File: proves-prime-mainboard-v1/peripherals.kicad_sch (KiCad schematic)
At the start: 38 parts, among them IC3 RV-3028-C7_32.768kHz_1ppm_TA_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, J6 Breakout, J7 Breakout, J8 Molex 503398-1892, U3 MCP25625-E/ML, U4 AP3602AKTR-G1, U5 LSM6DSOTR, U6 LSM303AGRTR, Y2 16MHZ 12 pf

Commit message: Migrated Temperature Sensor
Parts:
- added C38: 1uF, Capacitor_SMD:C_0805_2012Metric, symbol Device:C
- added U11: MCP9808T-E/MS, Package_SO:MSOP-8-1EP_3x3mm_P0.65mm_EP1.5x1.8mm_ThermalVias, symbol Sensor_Temperature:MCP9808_DFN
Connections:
- net +3V3: now also C38.1, U11.6 (A1), U11.7 (A0), U11.8 (VDD)
- net GND: now also C38.2, U11.4 (GND), U11.5 (A2), U11.9 (EP/GND)
- no-connect marks 23 -> 24
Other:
- moved on the sheet: C24, C25, C26, C27, C28, C31, C32, C33, C34, C35, D7, J6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

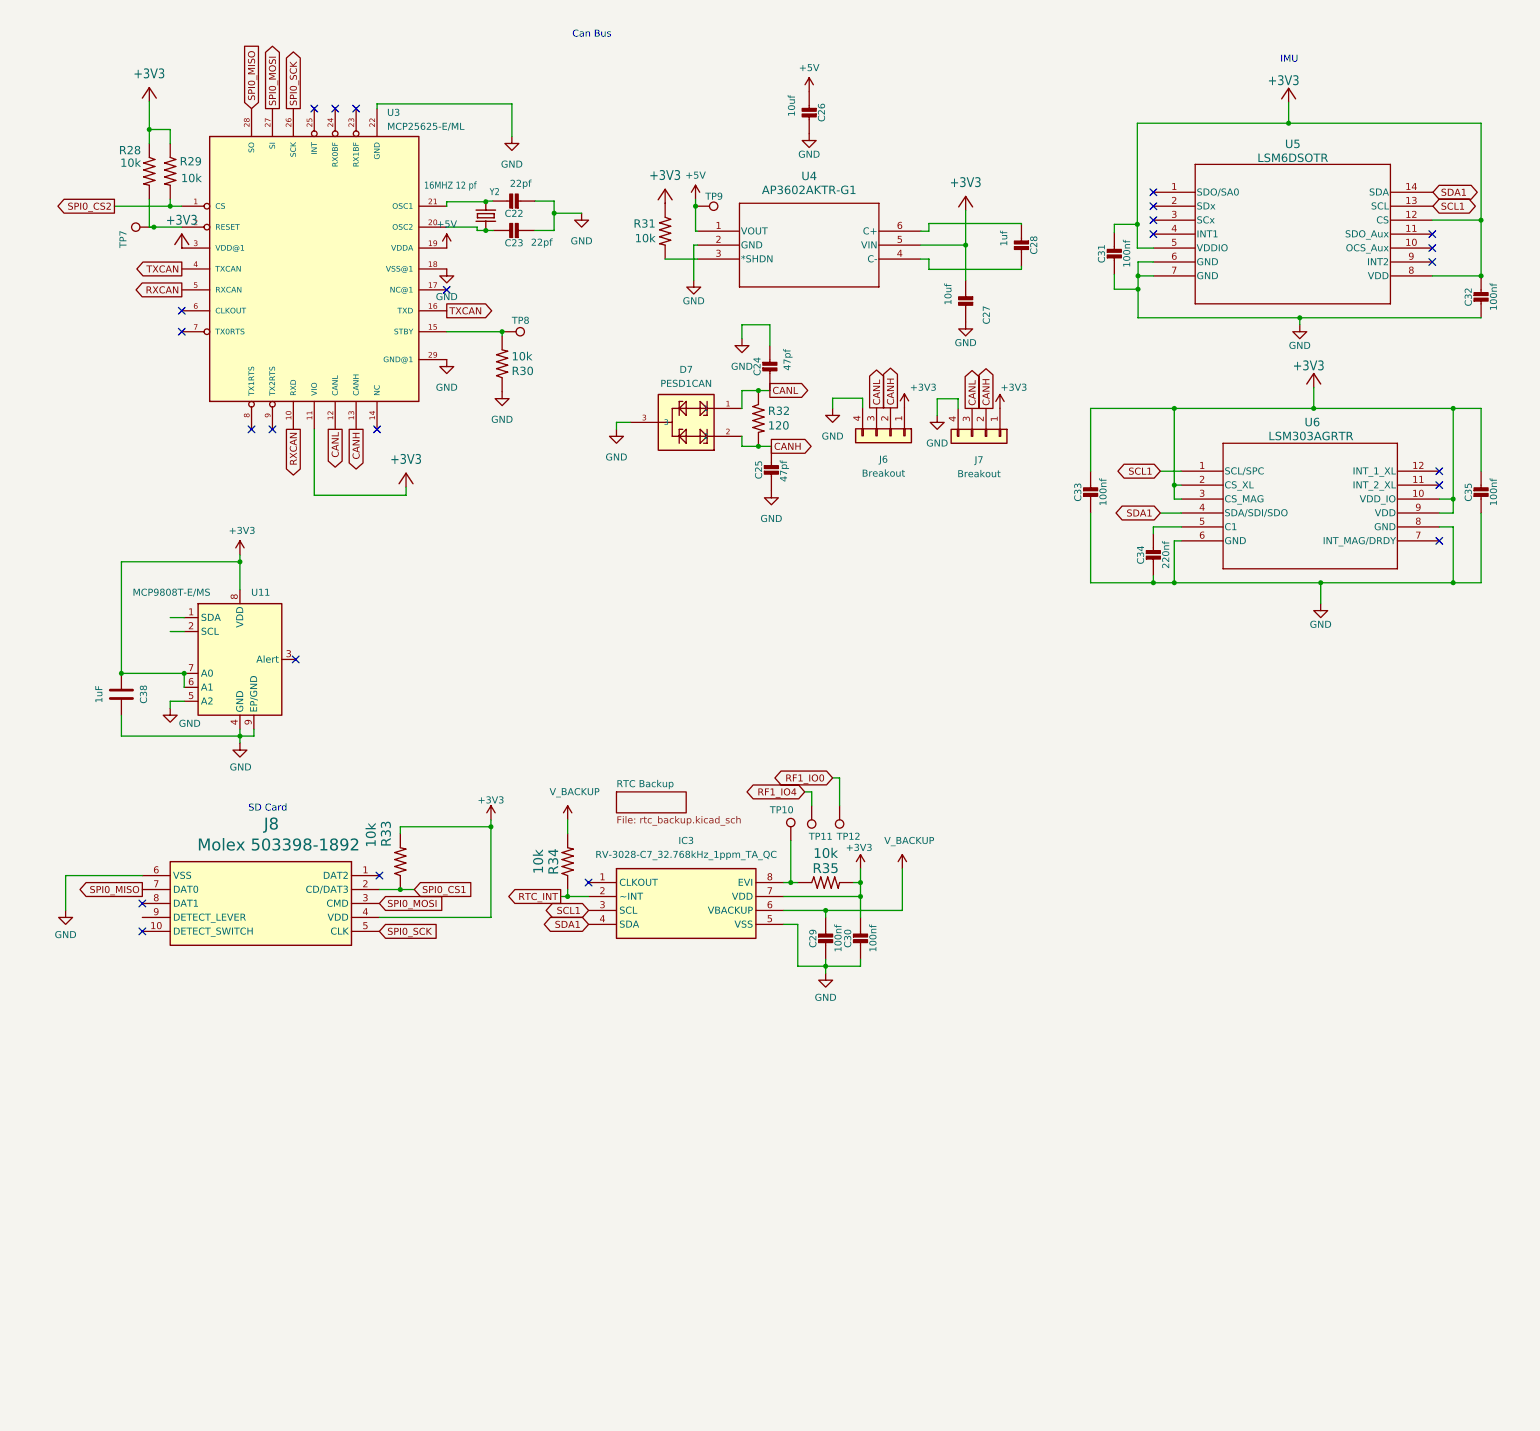
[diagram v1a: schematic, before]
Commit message: Added Voltage Regulators
LT8610 3v3 and 5v

Co-Authored-By: rrakushkin <128992626+rrakushkin@users.noreply.github.com>
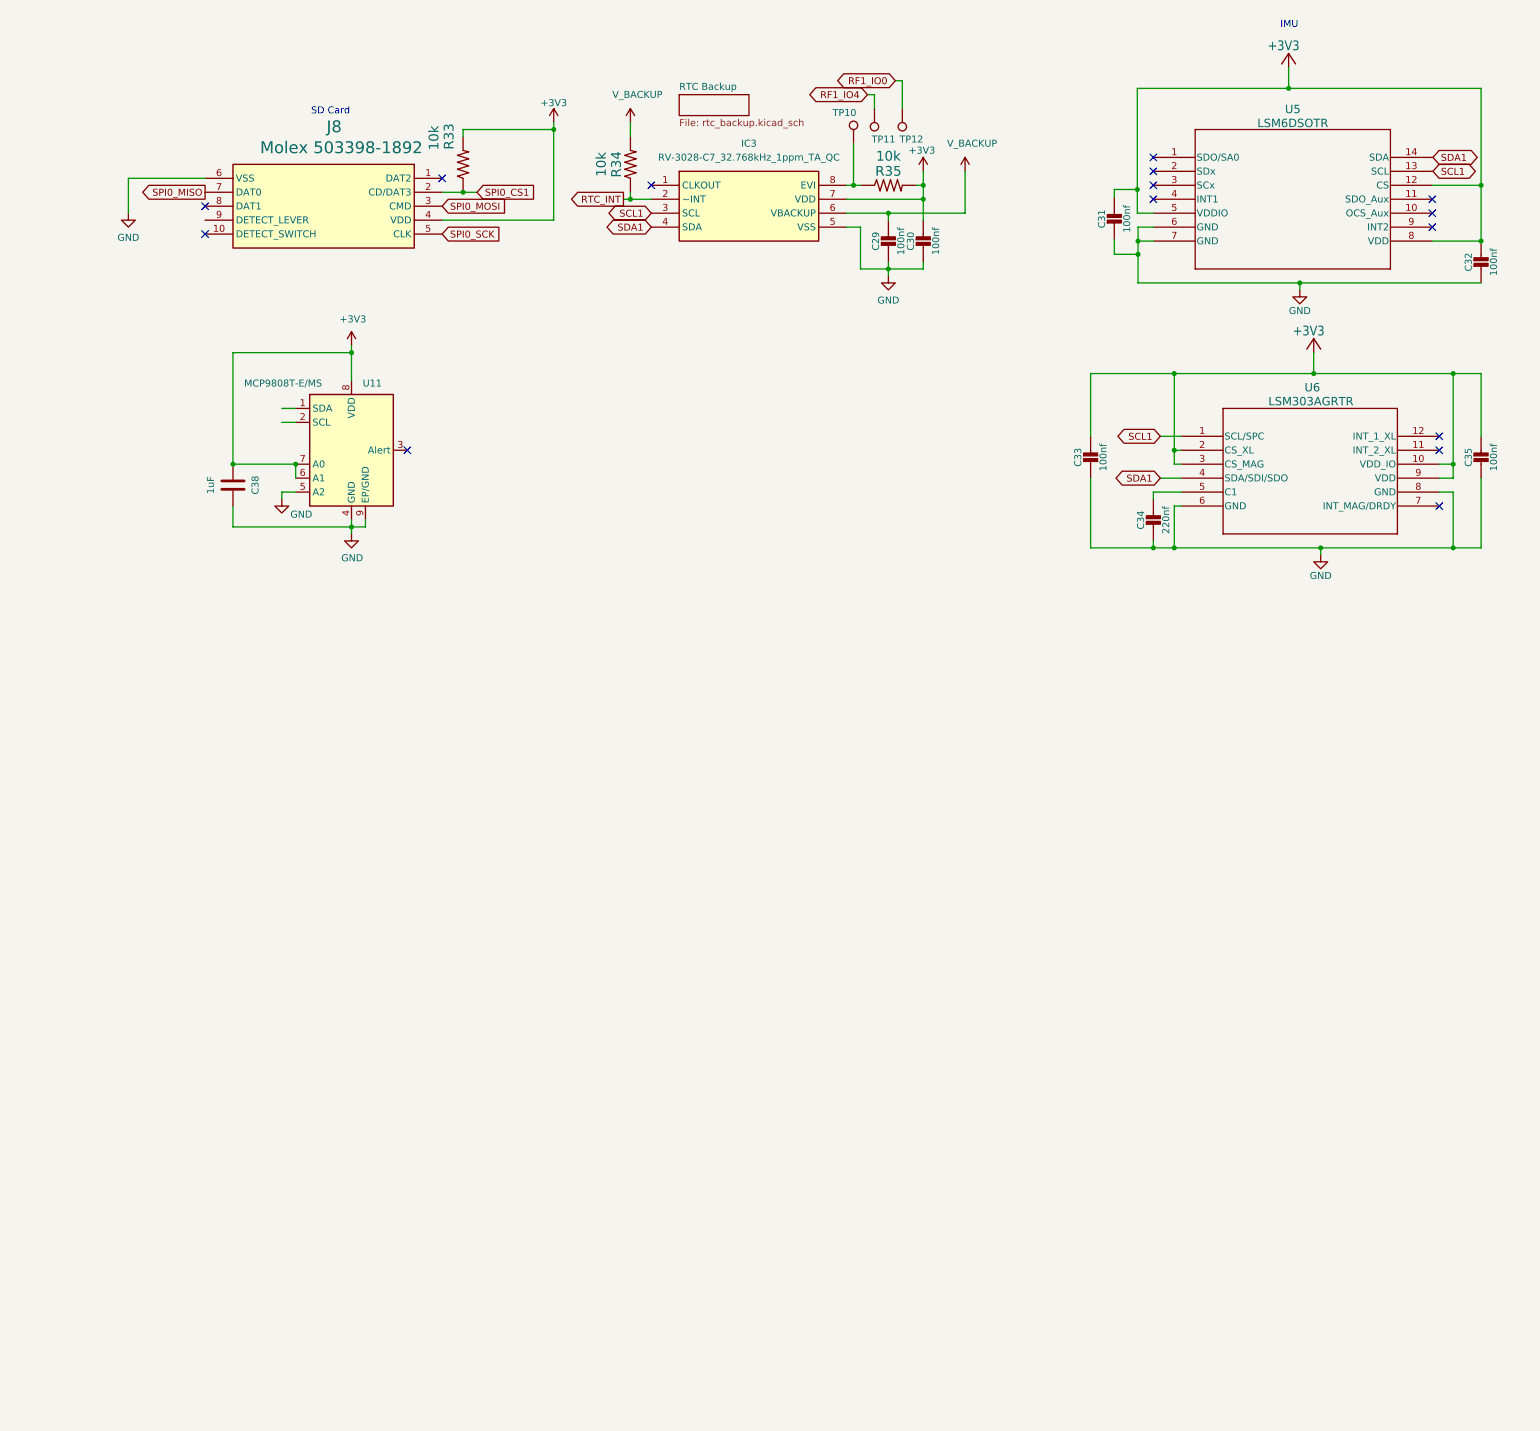
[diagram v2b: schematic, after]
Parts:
- removed C22, C23: 22pf, Capacitor_SMD:C_0402_1005Metric, symbol Adafruit Ethernet FeatherWing-eagle-import:CAP_CERAMIC0603_NO
- removed C24, C25: 47pf, Capacitor_SMD:C_0402_1005Metric, symbol Adafruit Ethernet FeatherWing-eagle-import:CAP_CERAMIC0603_NO
- removed C26, C27: 10uf, Capacitor_SMD:C_0603_1608Metric, symbol Adafruit Ethernet FeatherWing-eagle-import:CAP_CERAMIC0603_NO
- removed C28: 1uf, Capacitor_SMD:C_0603_1608Metric, symbol Adafruit Ethernet FeatherWing-eagle-import:CAP_CERAMIC0603_NO
- removed D7: PESD1CAN, Package_TO_SOT_SMD:SOT-23-3, symbol PESD1CAN:PESD1CAN
- removed J6, J7: Breakout, Connector_JST:JST_SH_BM04B-SRSS-TB_1x04-1MP_P1.00mm_Vertical, symbol Connector_Generic:Conn_01x04
- removed R28, R29, R30, R31: 10k, Resistor_SMD:R_0603_1608Metric, symbol mainboard:10KOHM-1_10W-1%(0603)0603
- removed R32: 120, Resistor_SMD:R_0603_1608Metric, symbol mainboard:10KOHM-1_10W-1%(0603)0603
- removed TP7: RESET, TestPoint:TestPoint_Loop_D1.80mm_Drill1.0mm_Beaded, symbol Connector:TestPoint
- removed TP8: Standby, TestPoint:TestPoint_Loop_D1.80mm_Drill1.0mm_Beaded, symbol Connector:TestPoint
- removed TP9: 5V, TestPoint:TestPoint_Loop_D1.80mm_Drill1.0mm_Beaded, symbol Connector:TestPoint
- removed U3: MCP25625-E/ML, Package_DFN_QFN:QFN-28-1EP_6x6mm_P0.65mm_EP4.25x4.25mm, symbol MCP25625-E_ML:MCP25625-E/ML
- removed U4: AP3602AKTR-G1, Package_TO_SOT_SMD:SOT-23-6, symbol AP3602:AP3602AKTR-G1
- removed Y2: 16MHZ 12 pf, Crystal:Crystal_SMD_2520-4Pin_2.5x2.0mm, symbol Adafruit ItsyBitsy RP2040-eagle-import:CRYSTAL2.5X2.0
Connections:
- no-connect marks 24 -> 15
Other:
- note removed: "Can Bus"
- moved on the sheet: C29, C30, C31, C32, C33, C34, C35, C38, IC3, J8, R33, R34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

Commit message: More Wiring!
Connected Additional Peripheral
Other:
- moved on the sheet: C38, U11
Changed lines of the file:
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@@
 	(paper "A4")
 	(junction
-		(at 67.31 106.68)
+		(at 63.5 97.79)
 		(diameter 0)
 		(color 0 0 0 0)
@@
 	)
 	(junction
-		(at 45.72 95.25)
+		(at 41.91 86.36)
 		(diameter 0)
 		(color 0 0 0 0)
@@
 	)
 	(junction
-		(at 57.15 95.25)
+		(at 63.5 68.58)
 		(diameter 0)
 		(color 0 0 0 0)
 	)
 	(junction
-		(at 237.998 26.797)
+		(at 53.34 86.36)
 		(diameter 0)
 		(color 0 0 0 0)
 	)
 	(junction
-		(at 171.45 46.99)
+		(at 237.998 26.797)
 		(diameter 0)
 		(color 0 0 0 0)
 	)
 	(junction
-		(at 213.36 110.49)
+		(at 171.45 46.99)
 		(diameter 0)
 		(color 0 0 0 0)
 	)
 	(junction
-		(at 67.31 74.93)
+		(at 213.36 110.49)
 		(diameter 0)
 		(color 0 0 0 0)
@@
 	)
 	(no_connect
-		(at 77.47 92.71)
+		(at 73.66 83.82)
 	)
 	(no_connect
@@
 	(wire
 		(pts
-			(xy 54.61 85.09) (xy 57.15 85.09)
+			(xy 50.8 76.2) (xy 53.34 76.2)
 		)
 		(stroke
@@
 	(wire
 		(pts
-			(xy 69.85 105.41) (xy 69.85 106.68)
+			(xy 66.04 96.52) (xy 66.04 97.79)
 		)
 		(stroke
@@
 	(wire
 		(pts
-			(xy 45.72 74.93) (xy 45.72 95.25)
+			(xy 41.91 68.58) (xy 41.91 86.36)
 		)
 		(stroke
@@
 	(wire
 		(pts
-			(xy 54.61 87.63) (xy 57.15 87.63)
+			(xy 50.8 78.74) (xy 53.34 78.74)
 		)
 		(stroke
@@
 	(wire
 		(pts
-			(xy 45.72 106.68) (xy 67.31 106.68)
+			(xy 41.91 97.79) (xy 63.5 97.79)
 		)
 		(stroke
@@
 	(wire
 		(pts
+			(xy 63.5 66.04) (xy 63.5 68.58)
+		)
+		(stroke
+			(width 0)
+			(type default)
+		)
+	)
+	(wire
+		(pts
 			(xy 264.16 54.61) (xy 273.05 54.61)
 		)
@@
 	(wire
 		(pts
-			(xy 57.15 95.25) (xy 45.72 95.25)
+			(xy 53.34 86.36) (xy 41.91 86.36)
 		)
 		(stroke
@@
 	(wire
 		(pts
-			(xy 67.31 106.68) (xy 67.31 107.95)
+			(xy 63.5 97.79) (xy 63.5 99.06)
 		)
 		(stroke
@@
 	(wire
 		(pts
-			(xy 57.15 100.33) (xy 54.61 100.33)
+			(xy 53.34 91.44) (xy 50.8 91.44)
 		)
 		(stroke
@@
 	(wire
 		(pts
-			(xy 57.15 95.25) (xy 57.15 97.79)
+			(xy 53.34 86.36) (xy 53.34 88.9)
 		)
 		(stroke
@@
 	(wire
 		(pts
-			(xy 45.72 106.68) (xy 45.72 102.87)
+			(xy 41.91 97.79) (xy 41.91 93.98)
 		)
 		(stroke
@@
 	(wire
 		(pts
-			(xy 67.31 106.68) (xy 67.31 105.41)
+			(xy 63.5 97.79) (xy 63.5 96.52)
 		)
 		(stroke
@@
 	(wire
 		(pts
-			(xy 67.31 74.93) (xy 67.31 80.01)
+			(xy 83.82 50.8) (xy 104.14 50.8)
 		)
 		(stroke
@@
 	(wire
 		(pts
-			(xy 83.82 50.8) (xy 104.14 50.8)
+			(xy 171.45 46.99) (xy 171.45 50.8)
 		)
 		(stroke
@@
 	(wire
 		(pts
-			(xy 171.45 46.99) (xy 171.45 50.8)
+			(xy 50.8 91.44) (xy 50.8 92.71)
 		)
 		(stroke
@@
 	(wire
 		(pts
-			(xy 54.61 100.33) (xy 54.61 101.6)
+			(xy 63.5 68.58) (xy 63.5 71.12)
 		)
 		(stroke
@@
 	(wire
 		(pts
-			(xy 69.85 106.68) (xy 67.31 106.68)
+			(xy 66.04 97.79) (xy 63.5 97.79)
 		)
 		(stroke
@@
 	(wire
 		(pts
-			(xy 67.31 73.66) (xy 67.31 74.93)
-		)
-		(stroke
-			(width 0)
-			(type default)
-		)
-	)
-	(wire
-		(pts
 			(xy 267.97 95.25) (xy 267.97 78.74)
 		)
@@
 	(wire
 		(pts
-			(xy 45.72 74.93) (xy 67.31 74.93)
+			(xy 41.91 68.58) (xy 63.5 68.58)
 		)
 		(stroke
@@
 	(symbol
 		(lib_id "Sensor_Temperature:MCP9808_DFN")
-		(at 67.31 92.71 0)
+		(at 63.5 83.82 0)
 		(unit 1)
 		(exclude_from_sim no)
@@
 		(dnp no)
 		(property "Reference" "U11"
-			(at 69.342 80.518 0)
+			(at 65.532 71.628 0)
 			(effects
 				(font
@@
 		)
 		(property "Value" "MCP9808T-E/MS"
-			(at 47.752 80.518 0)
+			(at 43.942 71.628 0)
 			(effects
 				(font
@@
 		)
 		(property "Footprint" "Package_SO:MSOP-8-1EP_3x3mm_P0.65mm_EP1.5x1.8mm_ThermalVias"
-			(at 67.31 92.71 0)
+			(at 63.5 83.82 0)
 			(effects
 				(font
@@
 		)
 		(property "Datasheet" "http://ww1.microchip.com/downloads/en/DeviceDoc/MCP9808-0.5C-Maximum-Accuracy-Digital-Temperature-Sensor-Data-Sheet-DS20005095B.pdf"
-			(at 60.96 81.28 0)
+			(at 57.15 72.39 0)
 			(effects
 				(font
@@
 		)
 		(property "Description" ""
-			(at 67.31 92.71 0)
+			(at 63.5 83.82 0)
 			(effects
 				(font
@@
 	(symbol
 		(lib_id "solar-panel-side-Z-rescue:+3.3V-power")
-		(at 67.31 73.66 0)
+		(at 63.5 66.04 0)
 		(unit 1)
 		(exclude_from_sim no)
@@
 		(dnp no)
 		(property "Reference" "#PWR078"
-			(at 67.31 77.47 0)
+			(at 63.5 69.85 0)
 			(effects
 				(font
@@
 		)
 		(property "Value" "+3V3"
-			(at 67.564 68.834 0)
+			(at 63.754 61.214 0)
 			(effects
 				(font
@@
 		)
 		(property "Footprint" ""
-			(at 67.31 73.66 0)
+			(at 63.5 66.04 0)
 			(effects
 				(font
@@
 		)
 		(property "Datasheet" ""
-			(at 67.31 73.66 0)
+			(at 63.5 66.04 0)
 			(effects
 				(font
@@
 		)
 		(property "Description" ""
-			(at 67.31 73.66 0)
+			(at 63.5 66.04 0)
 			(effects
 				(font
@@
 	(symbol
 		(lib_id "power:GND")
-		(at 67.31 107.95 0)
+		(at 63.5 99.06 0)
 		(unit 1)
 		(exclude_from_sim no)
@@
 		(dnp no)
 		(property "Reference" "#PWR079"
-			(at 67.31 114.3 0)
+			(at 63.5 105.41 0)
 			(effects
 				(font
@@
 		)
 		(property "Value" "GND"
-			(at 67.437 112.3442 0)
+			(at 63.627 103.4542 0)
 			(effects
 				(font
@@
 		)
 		(property "Footprint" ""
-			(at 67.31 107.95 0)
+			(at 63.5 99.06 0)
 			(effects
 				(font
@@
 		)
 		(property "Datasheet" ""
-			(at 67.31 107.95 0)
+			(at 63.5 99.06 0)
 			(effects
 				(font
@@
 		)
 		(property "Description" ""
-			(at 67.31 107.95 0)
+			(at 63.5 99.06 0)
 			(effects
 				(font
@@
 	(symbol
 		(lib_id "Device:C")
-		(at 45.72 99.06 0)
+		(at 41.91 90.17 0)
 		(unit 1)
 		(exclude_from_sim no)
@@
 		(dnp no)
 		(property "Reference" "C38"
-			(at 49.784 99.06 90)
+			(at 45.974 90.17 90)
 			(effects
 				(font
@@
 		)
 		(property "Value" "1uF"
-			(at 41.656 99.06 90)
+			(at 37.846 90.17 90)
 			(effects
 				(font
@@
 		)
 		(property "Footprint" "Capacitor_SMD:C_0805_2012Metric"
-			(at 46.6852 102.87 0)
+			(at 42.8752 93.98 0)
 			(effects
 				(font
@@
 		)
 		(property "Datasheet" "~"
-			(at 45.72 99.06 0)
+			(at 41.91 90.17 0)
 			(effects
 				(font
@@
 		)
 		(property "Description" ""
-			(at 45.72 99.06 0)
+			(at 41.91 90.17 0)
 			(effects
 				(font
@@
 	(symbol
 		(lib_id "power:GND")
-		(at 54.61 101.6 0)
+		(at 50.8 92.71 0)
 		(unit 1)
 		(exclude_from_sim no)
@@
 		(dnp no)
 		(property "Reference" "#PWR077"
-			(at 54.61 107.95 0)
+			(at 50.8 99.06 0)
 			(effects
 				(font
@@
 		)
 		(property "Value" "GND"
-			(at 58.166 104.394 0)
+			(at 54.356 95.504 0)
 			(effects
 				(font
@@
 		)
 		(property "Footprint" ""
-			(at 54.61 101.6 0)
+			(at 50.8 92.71 0)
 			(effects
 				(font
@@
 		)
 		(property "Datasheet" ""
-			(at 54.61 101.6 0)
+			(at 50.8 92.71 0)
 			(effects
 				(font
@@
 		)
 		(property "Description" ""
-			(at 54.61 101.6 0)
+			(at 50.8 92.71 0)
 			(effects
 				(font

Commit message: Added Mux
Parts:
- added R26, R27, R55: 10k, Resistor_SMD:R_Array_Convex_4x0603, symbol Device:R_Pack04
- added R51: 10K, Resistor_SMD:R_0603_1608Metric, symbol Device:R_US
- added U4: TCA9548APWR, TCA9548APWR:SOP65P640X120-24N, symbol TCA9548APWR:TCA9548APWR
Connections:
- net SCL1 is gone; now on net I2C0_SCL: IC3.3 (SCL), U5.13 (SCL), U6.1 (SCL/SPC)
- net SDA1 is gone; now on net I2C0_SDA: IC3.4 (SDA), U5.14 (SDA), U6.4 (SDA/SDI/SDO)
- net +3V3: now also R26.5 (R4.2), R26.6 (R3.2), R26.7 (R2.2), R26.8 (R1.2), R27.5 (R4.2), R27.6 (R3.2), R27.7 (R2.2), R27.8 (R1.2), R51.1, R55.5 (R4.2), R55.6 (R3.2), R55.7 (R2.2), R55.8 (R1.2), U4.1 (A0), U4.2 (A1), U4.21 (A2), U4.24 (VCC)
- net GND: now also U4.12 (GND)
- net I2C0_SDA: now reaches U11.1 (SDA)
- net I2C0_SCL: now reaches U11.2 (SCL)
- new net F0_SCL: R26.3 (R3.1), U4.5 (SC0)
- new net F0_SDA: R26.4 (R4.1), U4.4 (SD0)
- new net F1_SCL: R26.1 (R1.1), U4.7 (SC1)
- new net F1_SDA: R26.2 (R2.1), U4.6 (SD1)
- new net F2_SCL: R27.3 (R3.1), U4.9 (SC2)
- new net F2_SDA: R27.4 (R4.1), U4.8 (SD2)
- new net F3_SCL: R27.1 (R1.1), U4.11 (SC3)
- new net F3_SDA: R27.2 (R2.1), U4.10 (SD3)
- new net F4_SCL: R55.3 (R3.1), U4.14 (SC4)
- new net F4_SDA: R55.4 (R4.1), U4.13 (SD4)
- new net F5_SCL: R55.1 (R1.1), U4.16 (SC5)
- new net F5_SDA: R55.2 (R2.1), U4.15 (SD5)
- new net I2C1_SCL: U4.22 (SCL)
- new net I2C1_SDA: U4.23 (SDA)
- new net ~{MUX_RESET}: R51.2, U4.3 (~{RESET})
- no-connect marks 15 -> 19
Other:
- note added: "Sensor Multiplexer"
- moved on the sheet: C29, C30, C32, C38, IC3, J8, R33, R34, R35, TP10, TP11, TP12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
